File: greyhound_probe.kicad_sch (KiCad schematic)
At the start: 40 parts, among them J1 USB_C_Receptacle_USB2.0, J2 Conn_01x04_Male, J3 FTSH-105-01-L-DV-K-TR, Q1 IRLML6401, SW1 SW_SPDT, U1 XC6206P332MR, U2 USBLC6-2SC6, U3 STM32F072CBUx

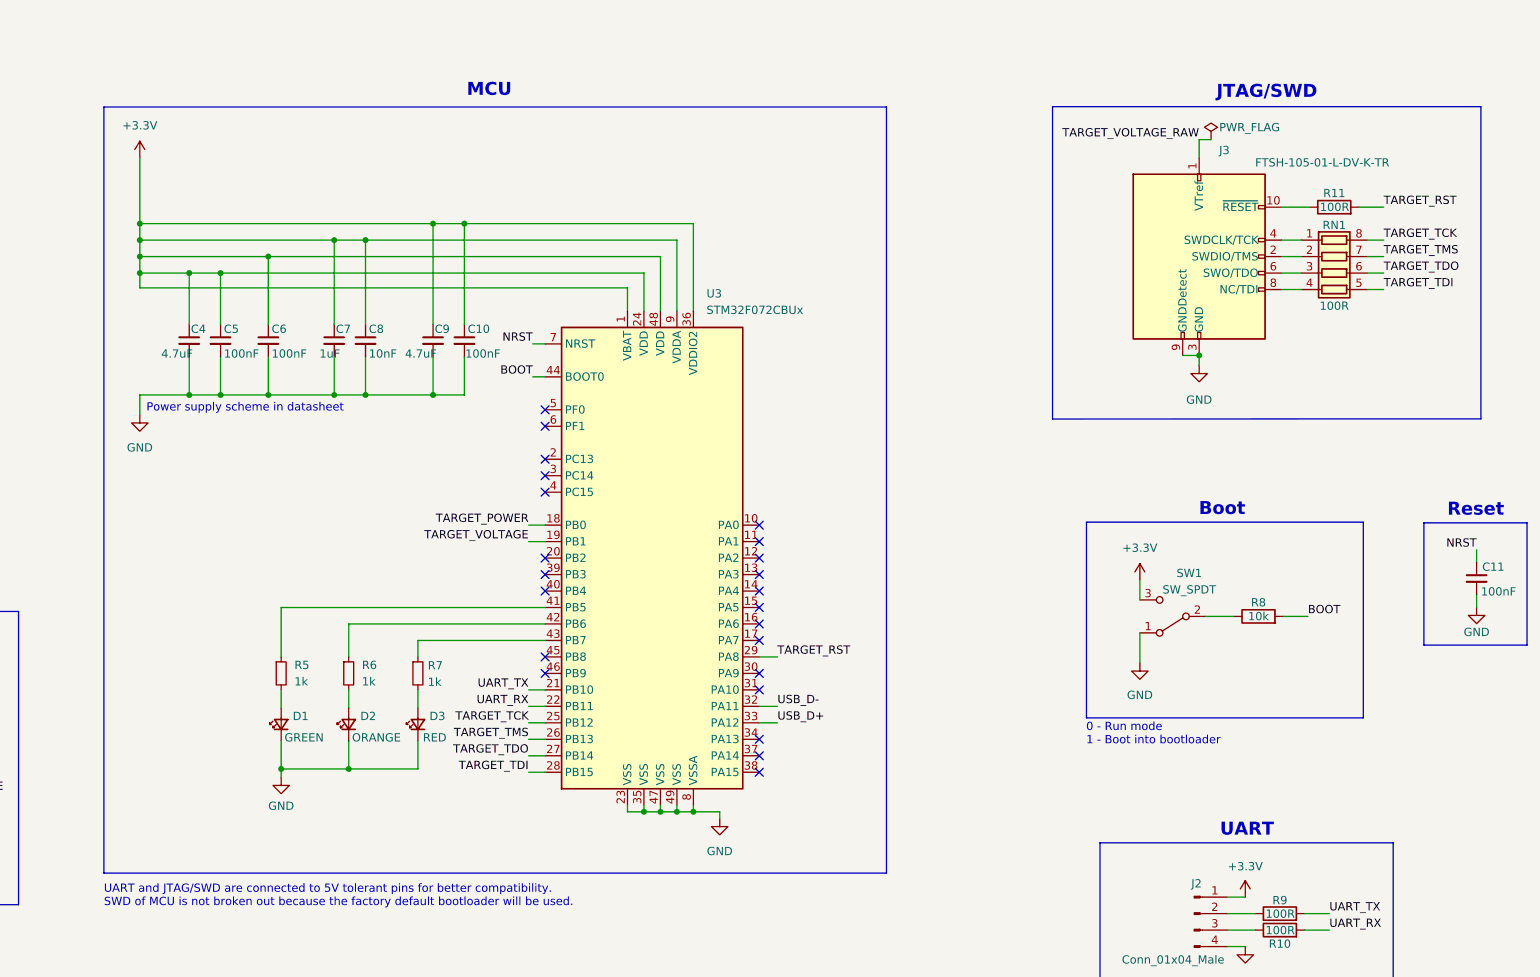
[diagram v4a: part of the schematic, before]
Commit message: PCB positioning changes, silkscreen changes
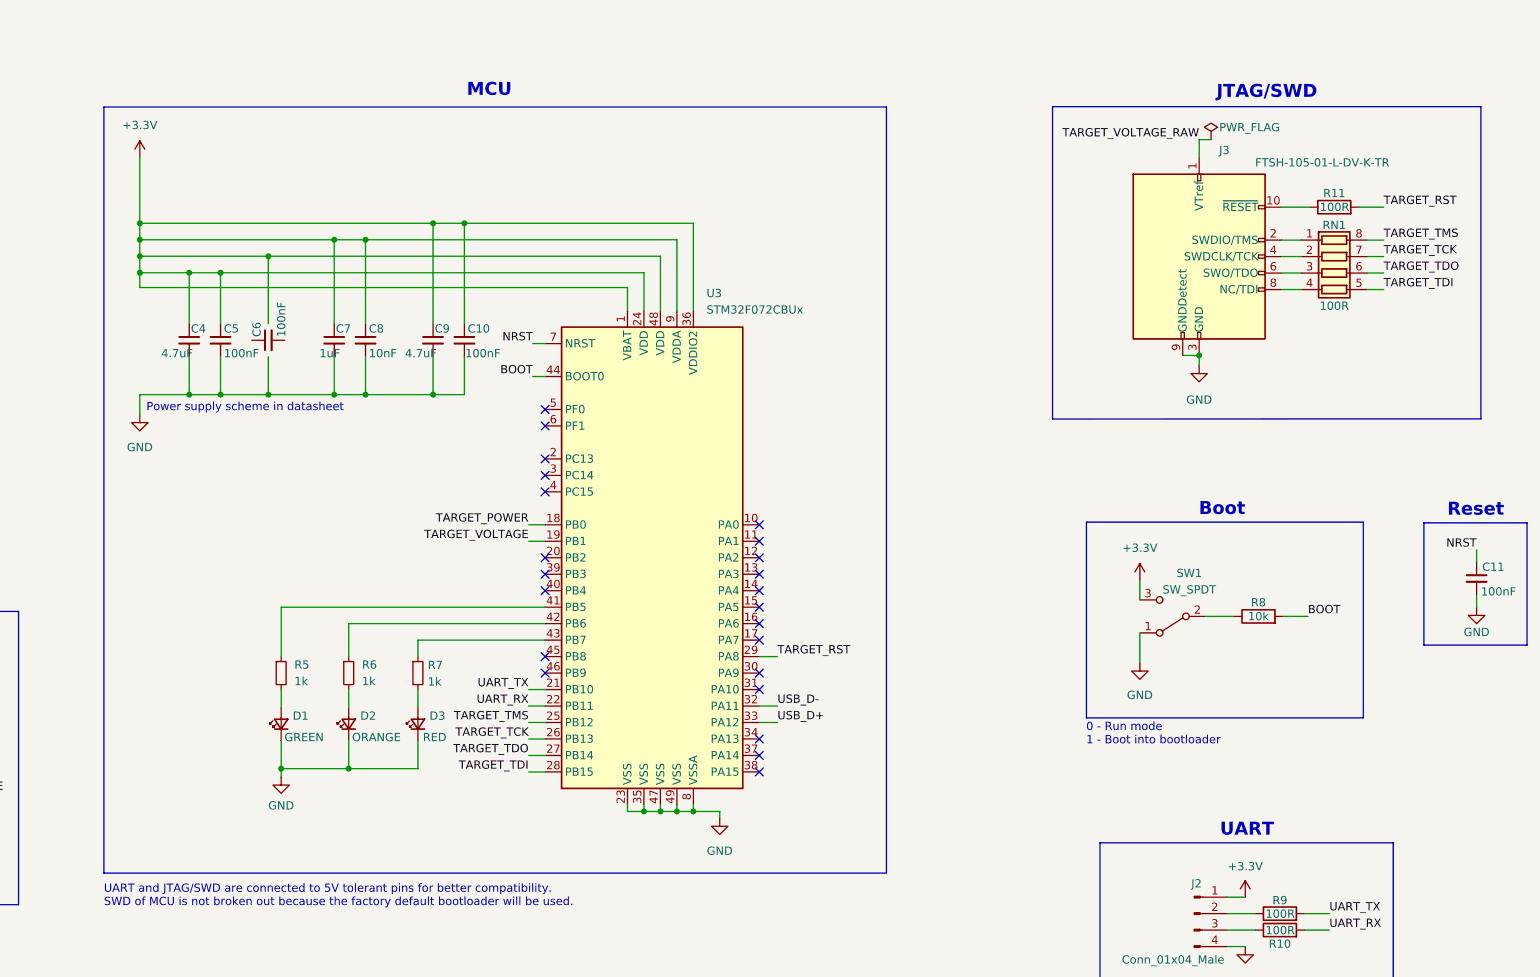
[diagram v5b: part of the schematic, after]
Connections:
- net +3.3V: no longer C6.1
- net GND: no longer C6.2
- net TARGET_TCK: now also RN1.7 (R2.2), U3.26 (PB13); no longer RN1.8 (R1.2), U3.25 (PB12)
- net TARGET_TMS: now also RN1.8 (R1.2), U3.25 (PB12); no longer RN1.7 (R2.2), U3.26 (PB13)
- net at RN1.1 (R1.1): now also J3.2 (SWDIO/TMS); no longer J3.4 (SWDCLK/TCK)
- net at RN1.2 (R2.1): now also J3.4 (SWDCLK/TCK); no longer J3.2 (SWDIO/TMS)
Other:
- moved on the sheet: C6

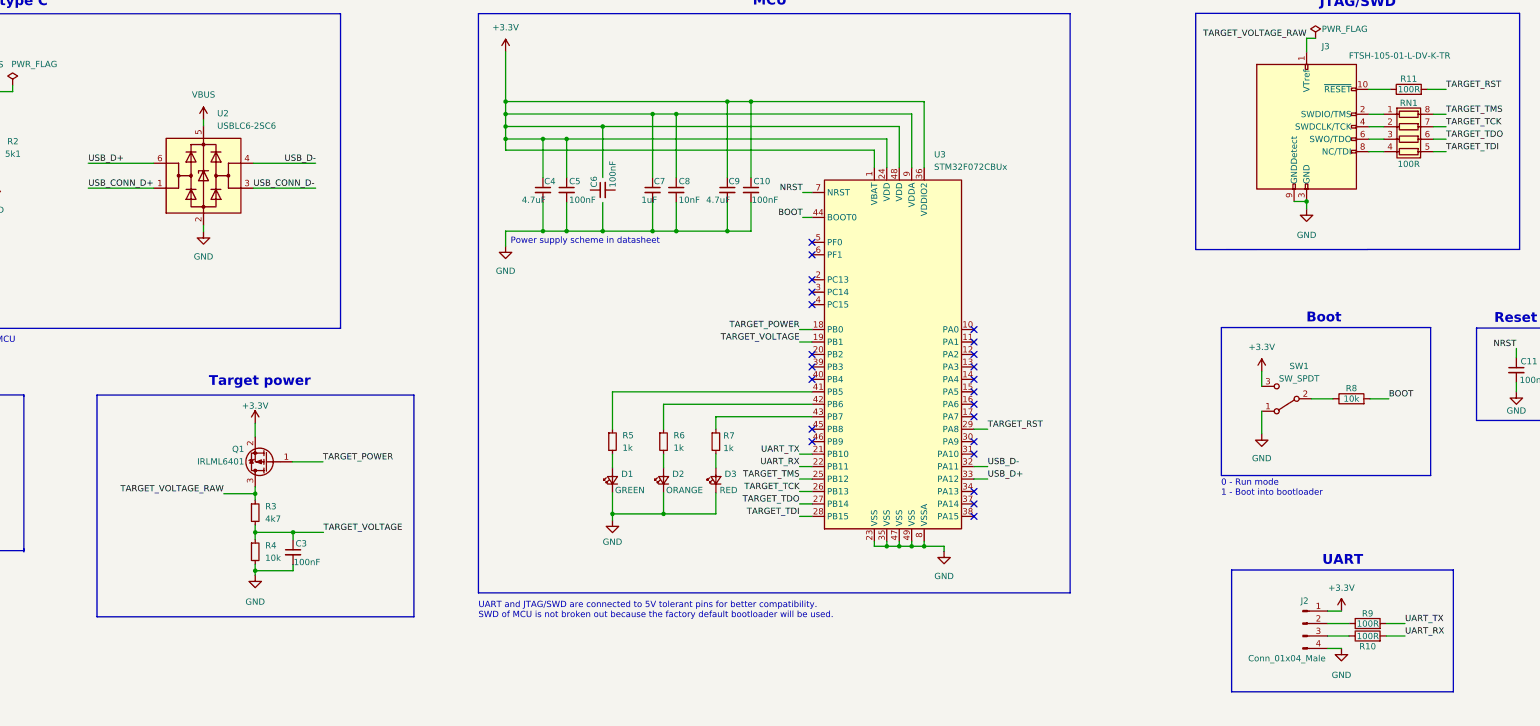
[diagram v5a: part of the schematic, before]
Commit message: Routing mostly done, rough board outline
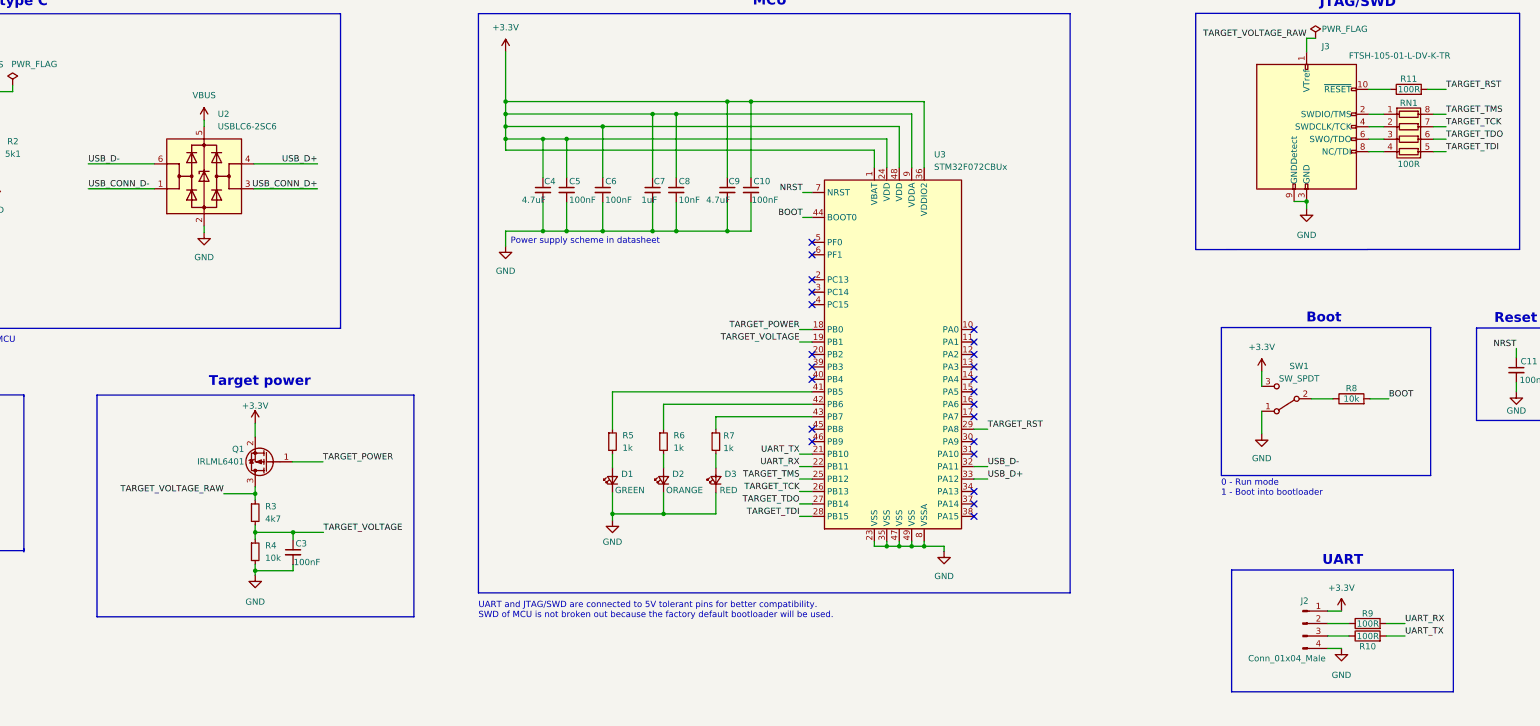
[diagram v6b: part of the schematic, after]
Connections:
- net +3.3V: now also C6.1
- net GND: now also C6.2
- net UART_RX: now also R9.2; no longer R10.2
- net UART_TX: now also R10.2; no longer R9.2
- net USB_CONN_D+: now also U2.3 (I/O2); no longer U2.1 (I/O1)
- net USB_CONN_D-: now also U2.1 (I/O1); no longer U2.3 (I/O2)
- net USB_D+: now also U2.4 (I/O2); no longer U2.6 (I/O1)
- net USB_D-: now also U2.6 (I/O1); no longer U2.4 (I/O2)
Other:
- moved on the sheet: C6
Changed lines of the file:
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@@
     (stroke (width 0) (type default) (color 0 0 0 0))
   )
-  (wire (pts (xy 121.539 78.613) (xy 121.539 79.883))
+  (wire (pts (xy 121.666 78.74) (xy 121.666 80.01))
     (stroke (width 0) (type default) (color 0 0 0 0))
   )
@@
     (stroke (width 0) (type default) (color 0 0 0 0))
   )
+  (wire (pts (xy 98.044 66.04) (xy 111.506 66.04))
+    (stroke (width 0) (type default) (color 0 0 0 0))
+  )
   (wire (pts (xy 52.832 65.278) (xy 66.802 65.278))
     (stroke (width 0) (type default) (color 0 0 0 0))
@@
     (stroke (width 0) (type default) (color 0 0 0 0))
   )
-  (wire (pts (xy 131.699 70.993) (xy 144.399 70.993))
+  (wire (pts (xy 131.826 71.12) (xy 144.78 71.12))
     (stroke (width 0) (type default) (color 0 0 0 0))
   )
@@
     (stroke (width 0) (type default) (color 0 0 0 0))
   )
-  (wire (pts (xy 98.044 70.993) (xy 111.379 70.993))
+  (wire (pts (xy 98.044 71.12) (xy 111.506 71.12))
     (stroke (width 0) (type default) (color 0 0 0 0))
   )
@@
     (stroke (width 0) (type default) (color 0 0 0 0))
   )
-  (wire (pts (xy 121.539 57.023) (xy 121.539 58.293))
+  (wire (pts (xy 121.666 57.15) (xy 121.666 58.42))
     (stroke (width 0) (type default) (color 0 0 0 0))
   )
@@
     (stroke (width 0) (type default) (color 0 0 0 0))
   )
-  (wire (pts (xy 131.699 65.913) (xy 144.399 65.913))
+  (wire (pts (xy 131.826 66.04) (xy 144.78 66.04))
     (stroke (width 0) (type default) (color 0 0 0 0))
   )
@@
   )
   (wire (pts (xy 350.774 159.766) (xy 355.092 159.766))
-    (stroke (width 0) (type default) (color 0 0 0 0))
-  )
-  (wire (pts (xy 98.044 65.913) (xy 111.379 65.913))
     (stroke (width 0) (type default) (color 0 0 0 0))
   )
@@
     (effects (font (size 1.27 1.27)) (justify right bottom))
   )
-  (label "USB_D-" (at 138.049 65.913 0)
+  (label "USB_D-" (at 98.044 66.04 0)
     (effects (font (size 1.27 1.27)) (justify left bottom))
   )
@@
     (effects (font (size 1.27 1.27)) (justify right bottom))
   )
-  (label "USB_D+" (at 98.044 65.913 0)
-    (effects (font (size 1.27 1.27)) (justify left bottom))
+  (label "USB_D+" (at 144.78 66.04 180)
+    (effects (font (size 1.27 1.27)) (justify right bottom))
   )
   (label "TARGET_RST" (at 281.432 120.142 0)
@@
     (effects (font (size 1.27 1.27)) (justify left bottom))
   )
-  (label "UART_TX" (at 366.522 159.766 0)
+  (label "UART_TX" (at 366.522 162.306 0)
     (effects (font (size 1.27 1.27)) (justify left bottom))
   )
@@
     (effects (font (size 1.27 1.27)) (justify left bottom))
   )
-  (label "UART_RX" (at 366.522 162.306 0)
-    (effects (font (size 1.27 1.27)) (justify left bottom))
-  )
-  (label "USB_CONN_D-" (at 131.699 70.993 0)
+  (label "UART_RX" (at 366.522 159.766 0)
+    (effects (font (size 1.27 1.27)) (justify left bottom))
+  )
+  (label "USB_CONN_D-" (at 98.044 71.12 0)
     (effects (font (size 1.27 1.27)) (justify left bottom))
   )
@@
     (effects (font (size 1.27 1.27)) (justify left bottom))
   )
-  (label "USB_CONN_D+" (at 98.044 70.993 0)
-    (effects (font (size 1.27 1.27)) (justify left bottom))
+  (label "USB_CONN_D+" (at 144.78 71.12 180)
+    (effects (font (size 1.27 1.27)) (justify right bottom))
   )
   (symbol (lib_id "Device:R") (at 358.902 159.766 90) (unit 1)
@@
     (pin "9")
   )
-  (symbol (lib_id "Power_Protection:USBLC6-2SC6") (at 121.539 68.453 0) (unit 1)
-    (in_bom yes) (on_board yes) (fields_autoplaced)
-    (property "Reference" "U2" (id 0) (at 124.3077 55.753 0)
-      (effects (font (size 1.27 1.27)) (justify left))
-    )
-    (property "Value" "USBLC6-2SC6" (id 1) (at 124.3077 58.293 0)
-      (effects (font (size 1.27 1.27)) (justify left))
-    )
-    (property "Footprint" "Package_TO_SOT_SMD:SOT-23-6" (id 2) (at 121.539 81.153 0)
-      (effects (font (size 1.27 1.27)) hide)
-    )
-    (property "Datasheet" "https://www.st.com/resource/en/datasheet/usblc6-2.pdf" (id 3) (at 126.619 59.563 0)
-      (effects (font (size 1.27 1.27)) hide)
-    )
-    (property "LCSC Part" "C2827654" (id 4) (at 121.539 68.453 0)
+  (symbol (lib_id "Power_Protection:USBLC6-2SC6") (at 121.666 68.58 0) (unit 1)
+    (in_bom yes) (on_board yes) (fields_autoplaced)
+    (property "Reference" "U2" (id 0) (at 124.4347 55.88 0)
+      (effects (font (size 1.27 1.27)) (justify left))
+    )
+    (property "Value" "USBLC6-2SC6" (id 1) (at 124.4347 58.42 0)
+      (effects (font (size 1.27 1.27)) (justify left))
+    )
+    (property "Footprint" "Package_TO_SOT_SMD:SOT-23-6" (id 2) (at 121.666 81.28 0)
+      (effects (font (size 1.27 1.27)) hide)
+    )
+    (property "Datasheet" "https://www.st.com/resource/en/datasheet/usblc6-2.pdf" (id 3) (at 126.746 59.69 0)
+      (effects (font (size 1.27 1.27)) hide)
+    )
+    (property "LCSC Part" "C2827654" (id 4) (at 121.666 68.58 0)
       (effects (font (size 1.27 1.27)) hide)
     )
@@
     (pin "1")
   )
-  (symbol (lib_id "power:GND") (at 121.539 79.883 0) (unit 1)
-    (in_bom yes) (on_board yes) (fields_autoplaced)
-    (property "Reference" "#PWR010" (id 0) (at 121.539 86.233 0)
-      (effects (font (size 1.27 1.27)) hide)
-    )
-    (property "Value" "GND" (id 1) (at 121.539 84.963 0))
-    (property "Footprint" "" (id 2) (at 121.539 79.883 0)
-      (effects (font (size 1.27 1.27)) hide)
-    )
-    (property "Datasheet" "" (id 3) (at 121.539 79.883 0)
+  (symbol (lib_id "power:GND") (at 121.666 80.01 0) (unit 1)
+    (in_bom yes) (on_board yes) (fields_autoplaced)
+    (property "Reference" "#PWR010" (id 0) (at 121.666 86.36 0)
+      (effects (font (size 1.27 1.27)) hide)
+    )
+    (property "Value" "GND" (id 1) (at 121.666 85.09 0))
+    (property "Footprint" "" (id 2) (at 121.666 80.01 0)
+      (effects (font (size 1.27 1.27)) hide)
+    )
+    (property "Datasheet" "" (id 3) (at 121.666 80.01 0)
       (effects (font (size 1.27 1.27)) hide)
     )
@@
     )
   )
-  (symbol (lib_id "power:VBUS") (at 121.539 57.023 0) (unit 1)
-    (in_bom yes) (on_board yes) (fields_autoplaced)
-    (property "Reference" "#PWR09" (id 0) (at 121.539 60.833 0)
-      (effects (font (size 1.27 1.27)) hide)
-    )
-    (property "Value" "VBUS" (id 1) (at 121.539 51.943 0))
-    (property "Footprint" "" (id 2) (at 121.539 57.023 0)
-      (effects (font (size 1.27 1.27)) hide)
-    )
-    (property "Datasheet" "" (id 3) (at 121.539 57.023 0)
+  (symbol (lib_id "power:VBUS") (at 121.666 57.15 0) (unit 1)
+    (in_bom yes) (on_board yes) (fields_autoplaced)
+    (property "Reference" "#PWR09" (id 0) (at 121.666 60.96 0)
+      (effects (font (size 1.27 1.27)) hide)
+    )
+    (property "Value" "VBUS" (id 1) (at 121.666 52.07 0))
+    (property "Footprint" "" (id 2) (at 121.666 57.15 0)
+      (effects (font (size 1.27 1.27)) hide)
+    )
+    (property "Datasheet" "" (id 3) (at 121.666 57.15 0)
       (effects (font (size 1.27 1.27)) hide)
     )
@@
     (pin "2")
   )
-  (symbol (lib_id "Device:C_Small") (at 202.946 71.374 90) (unit 1)
-    (in_bom yes) (on_board yes)
-    (property "Reference" "C6" (id 0) (at 201.168 70.866 0)
-      (effects (font (size 1.27 1.27)) (justify left))
-    )
-    (property "Value" "100nF" (id 1) (at 204.978 70.866 0)
-      (effects (font (size 1.27 1.27)) (justify left))
-    )
+  (symbol (lib_id "Device:C_Small") (at 202.946 71.374 0) (unit 1)
+    (in_bom yes) (on_board yes)
+    (property "Reference" "C6" (id 0) (at 203.454 69.596 0)
+      (effects (font (size 1.27 1.27)) (justify left))
+    )
+    (property "Value" "100nF" (id 1) (at 203.454 73.406 0)
+      (effects (font (size 1.27 1.27)) (justify left))
+    )
